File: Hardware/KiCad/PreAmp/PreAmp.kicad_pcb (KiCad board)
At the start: 2 copper layers, 27 parts, among them J1 XLR3, J2 Conn_01x03_Pin, J3 Conn_01x05_Pin, U1 TLV2371DBV, U2 INA217AIDWR

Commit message: Layout everything globaly
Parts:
- moved R4 66.8 mm to (172.8, 67.0), turned to 90 degrees
- moved R2 51.6 mm to (160.2, 57.5), turned to 0 degrees
- moved TP2 47.6 mm to (172.0, 84.2)
- moved R1 46.9 mm to (156.1, 57.5), turned to 0 degrees
- moved U1 45.7 mm to (158.3, 61.2), turned to 90 degrees
- moved J3 44.3 mm to (140.5, 52.5)
- moved C4 43.2 mm to (151.2, 71.2)
- moved U2 41.8 mm to (158.8, 69.8)
- moved TP3 41.8 mm to (149.8, 67.5)
- moved TP1 41.7 mm to (153.5, 62.2)
- moved C3 40.1 mm to (166.0, 65.2), turned to 90 degrees
- moved J2 39.9 mm to (140.5, 68.5)
- moved R3 39.2 mm to (172.8, 73.3), turned to -90 degrees
- moved R5 21.8 mm to (151.2, 75.2), turned to -90 degrees
- moved RV1 21.2 mm to (161.2, 77.2)
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
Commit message: First layout
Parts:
- removed J3: Conn_01x05_Pin, Connector_PinSocket_2.54mm:PinSocket_1x05_P2.54mm_Vertical
- J2: value Conn_01x03_Pin -> Conn_01x05_Pin; footprint Connector_PinSocket_2.54mm:PinSocket_1x03_P2.54mm_Vertical -> Connector_PinHeader_2.54mm:PinHeader_1x05_P2.54mm_Vertical
- moved J2 5.09 mm to (145.5, 67.5), turned to 180 degrees
- moved D1 0.26 mm to (180.2, 60.4)
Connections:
- J2 pad 1: GND -> Out
- J2 pad 2: Out -> GND
- J2 pad 3: GND -> -6V

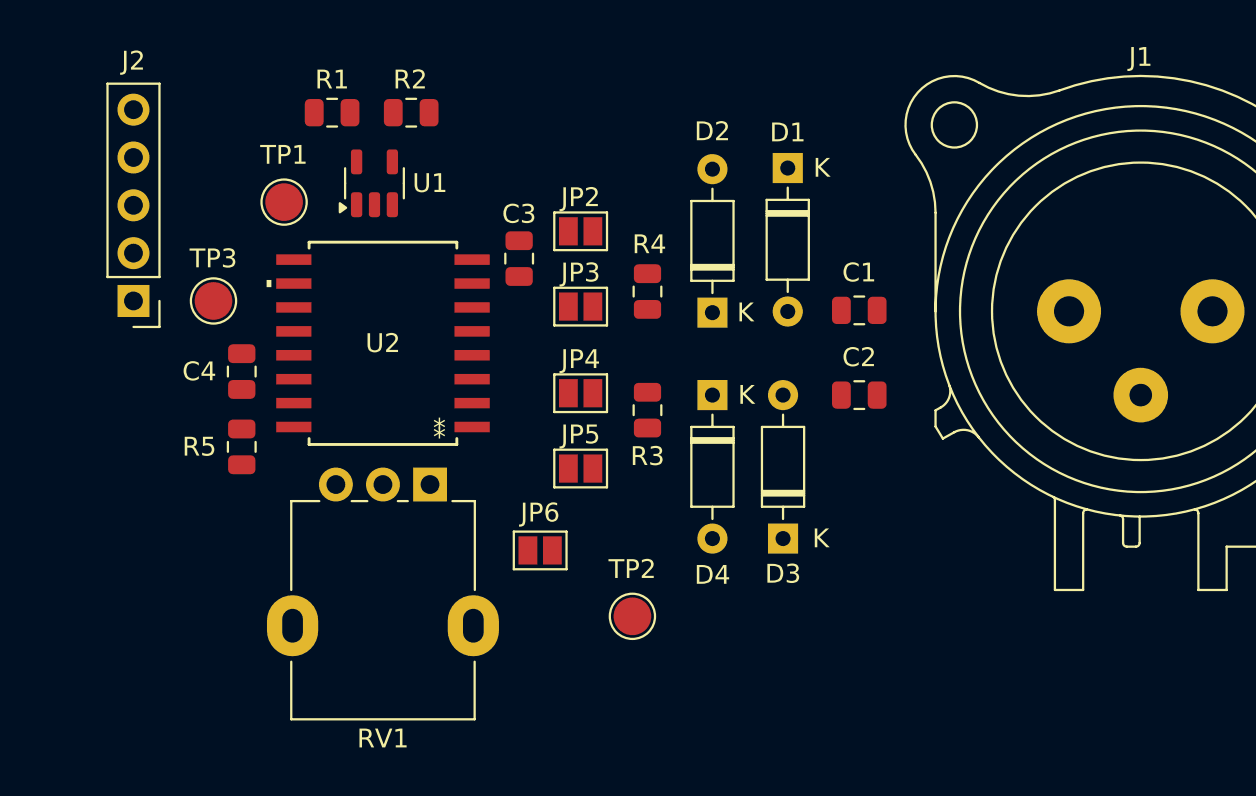
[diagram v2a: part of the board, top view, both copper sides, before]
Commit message: Equal length traces for Hot and Cold
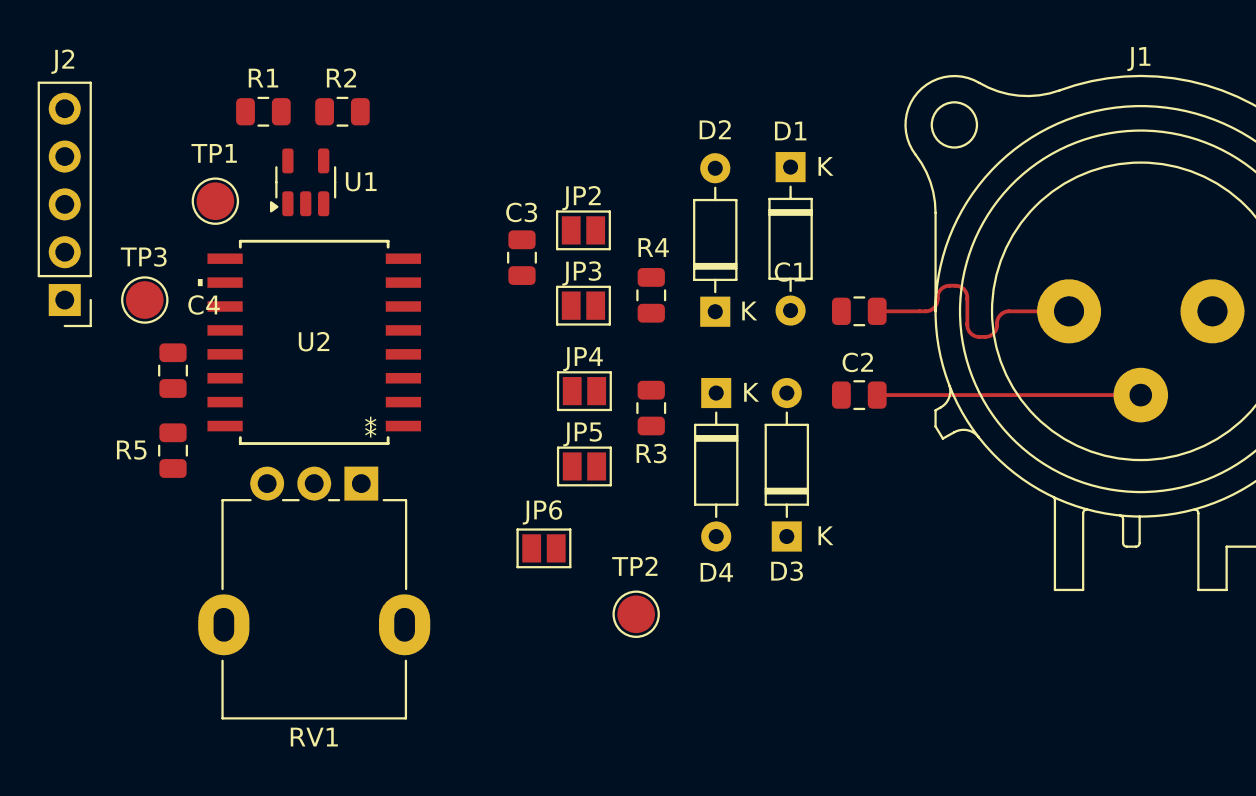
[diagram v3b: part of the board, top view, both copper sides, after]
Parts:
- moved R5 3.66 mm to (147.6, 75.5), turned to 90 degrees
- moved C4 3.65 mm to (147.6, 71.2)
- moved J2 3.65 mm to (141.8, 67.5)
- moved R1 3.65 mm to (152.4, 57.5)
- moved R2 3.65 mm to (156.6, 57.5)
- moved RV1 3.65 mm to (157.6, 77.2)
- moved TP1 3.65 mm to (149.8, 62.2)
- moved TP3 3.65 mm to (146.1, 67.5)
- moved U1 3.65 mm to (154.7, 61.2)
- moved U2 3.65 mm to (155.1, 69.7)
- moved R4 0.28 mm to (173.0, 67.2)
- moved JP6 0.23 mm to (167.3, 80.6)
- moved D3 0.23 mm to (180.2, 80.0)
- moved D4 0.23 mm to (176.4, 72.4)
- moved JP4 0.23 mm to (169.4, 72.3)
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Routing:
- net Cold: track 0.00 -> 14.0 mm
- net Hot: track 0.00 -> 13.8 mm

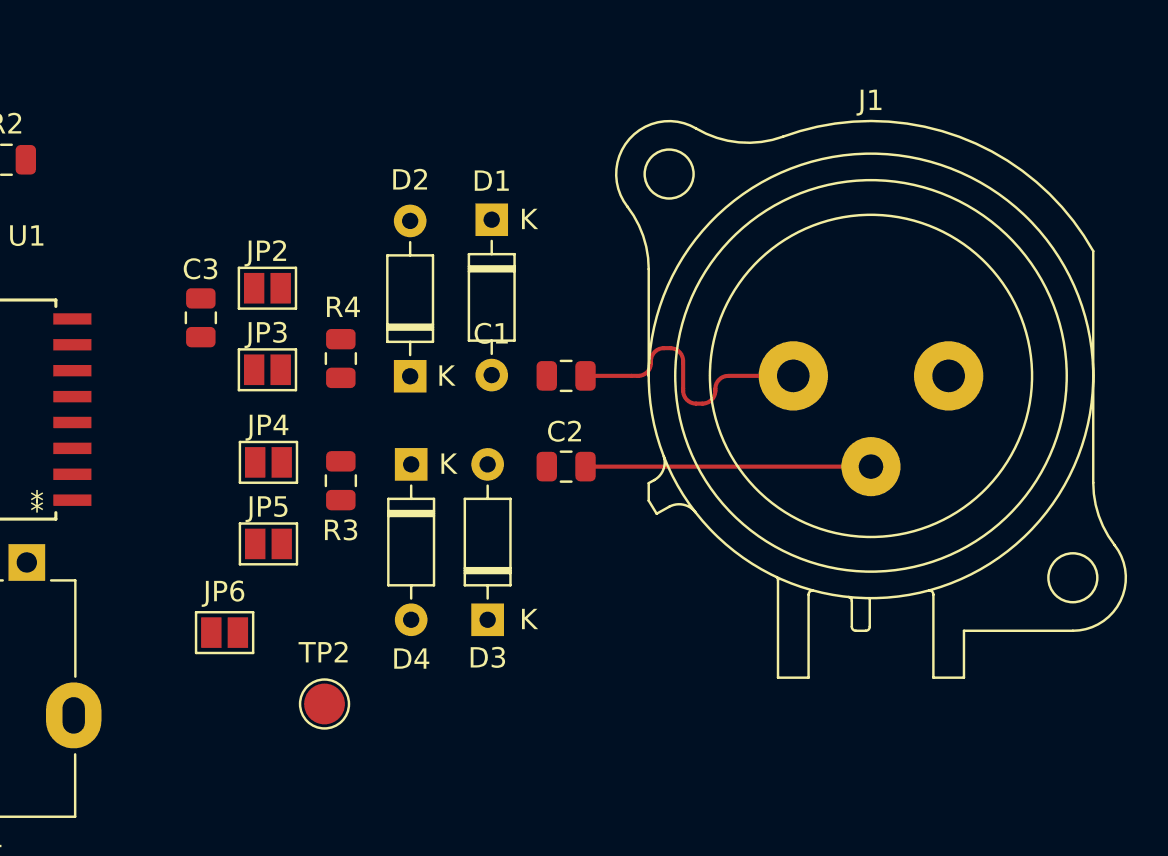
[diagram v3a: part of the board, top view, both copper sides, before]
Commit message: First part of differential routing
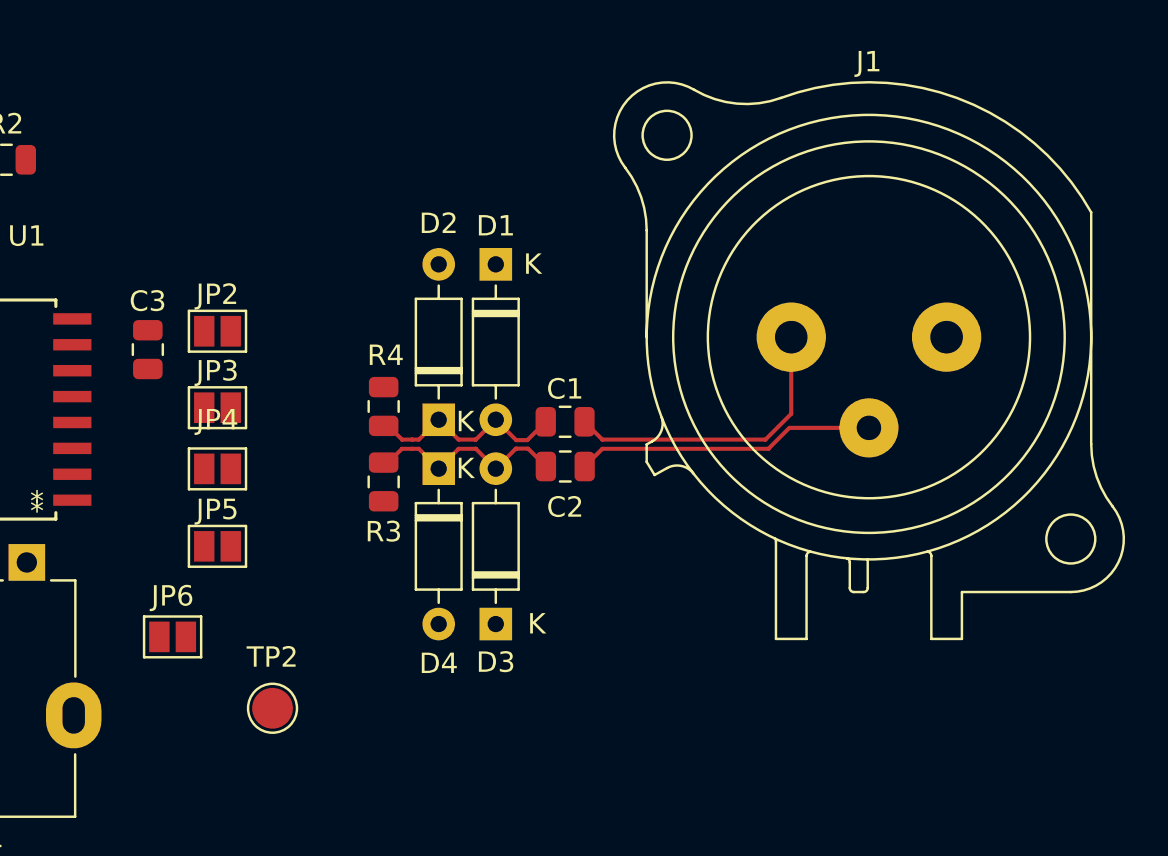
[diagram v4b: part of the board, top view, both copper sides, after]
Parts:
- moved JP2 3.23 mm to (166.9, 65.9)
- moved R4 3.15 mm to (175.1, 69.5)
- moved JP3 3.08 mm to (166.9, 69.6)
- moved C3 3.03 mm to (163.5, 66.8)
- moved JP6 2.56 mm to (164.8, 80.8)
- moved TP2 2.56 mm to (169.7, 84.3)
- moved D2 2.55 mm to (177.8, 70.2)
- moved JP4 2.52 mm to (166.9, 72.6)
- moved JP5 2.50 mm to (166.9, 76.4)
- moved C1 2.25 mm to (184.0, 70.3)
- moved D1 2.20 mm to (180.6, 62.6)
- moved R3 2.10 mm to (175.1, 73.2)
- moved J1 1.90 mm to (202.7, 66.2)
- moved D4 1.37 mm to (177.8, 72.6)
- moved D3 0.45 mm to (180.6, 80.2)
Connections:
- net Cold renamed Input-
- net Hot renamed Input+
- net Net-(D1-A) renamed /In+
- net Net-(D3-A) renamed /In-
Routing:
- net /In+: track 0.00 -> 10.6 mm
- net /In-: track 0.00 -> 10.2 mm
- net Input+: track 13.8 -> 14.8 mm
- net Input-: track 14.0 -> 14.7 mm

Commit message: Removed 4 jumper points
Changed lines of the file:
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@@
 			(layer "F.Fab")
-		)
-		(fp_text user "K"
-			(at 0 -1.3 180)
-			(layer "F.SilkS")
-			(effects
-				(font
-					(size 1 1)
-					(thickness 0.15)
-				)
-			)
 		)
 		(fp_text user "${REFERENCE}"
@@
 		)
 		(fp_text user "K"
-			(at -0.1 1.3 180)
-			(layer "F.SilkS")
-			(effects
-				(font
-					(size 1 1)
-					(thickness 0.15)
-				)
-			)
-		)
-		(fp_text user "K"

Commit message: Connected everything together
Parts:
- removed JP2, JP3, JP4, JP5: SolderJumper_2_Open, Jumper:SolderJumper-2_P1.3mm_Open_Pad1.0x1.5mm
- moved TP2 29.0 mm to (198.5, 87.4)
- moved J2 11.2 mm to (152.9, 69.4)
- moved TP3 10.9 mm to (156.8, 69.4)
- moved C4 10.7 mm to (158.1, 73.0)
- moved R5 10.3 mm to (157.8, 77.0)
- moved U2 10.2 mm to (165.2, 71.4)
- moved RV1 10.2 mm to (167.7, 78.4)
- moved TP1 9.46 mm to (159.2, 63.9)
- moved JP1 9.27 mm to (173.9, 79.7)
- moved C3 8.88 mm to (172.4, 66.2)
- moved R2 8.13 mm to (164.7, 57.2)
- moved R1 8.13 mm to (160.5, 57.2)
- moved U1 8.13 mm to (162.8, 61.0)
- moved J1 0.45 mm to (203.1, 66.0)
- moved C1 0.40 mm to (184.4, 70.3)
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- renumbered JP6 to JP1
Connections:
- net Input+ renamed /Input+
- net Input- renamed /Input-
- U2 pad 4: Net-(JP4-B) -> /In-
- U2 pad 5: Net-(JP2-B) -> /In+
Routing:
- net -6V: track 0.00 -> 56.5 mm, vias 0 -> 2
- net 6V: track 0.00 -> 32.8 mm
- net 1.6V: track 0.00 -> 15.2 mm
- net Out: track 0.00 -> 7.60 mm
- net Net-(U2-RG1): track 0.00 -> 6.32 mm
- net Net-(JP1-A): track 0.00 -> 6.14 mm
- net /In+: track 10.6 -> 16.6 mm
- net /In-: track 10.2 -> 16.3 mm
- net Net-(R5-Pad1): track 0.00 -> 5.07 mm
- net Net-(U1--): track 0.00 -> 4.93 mm
- net Net-(U2-RG2): track 0.00 -> 3.36 mm

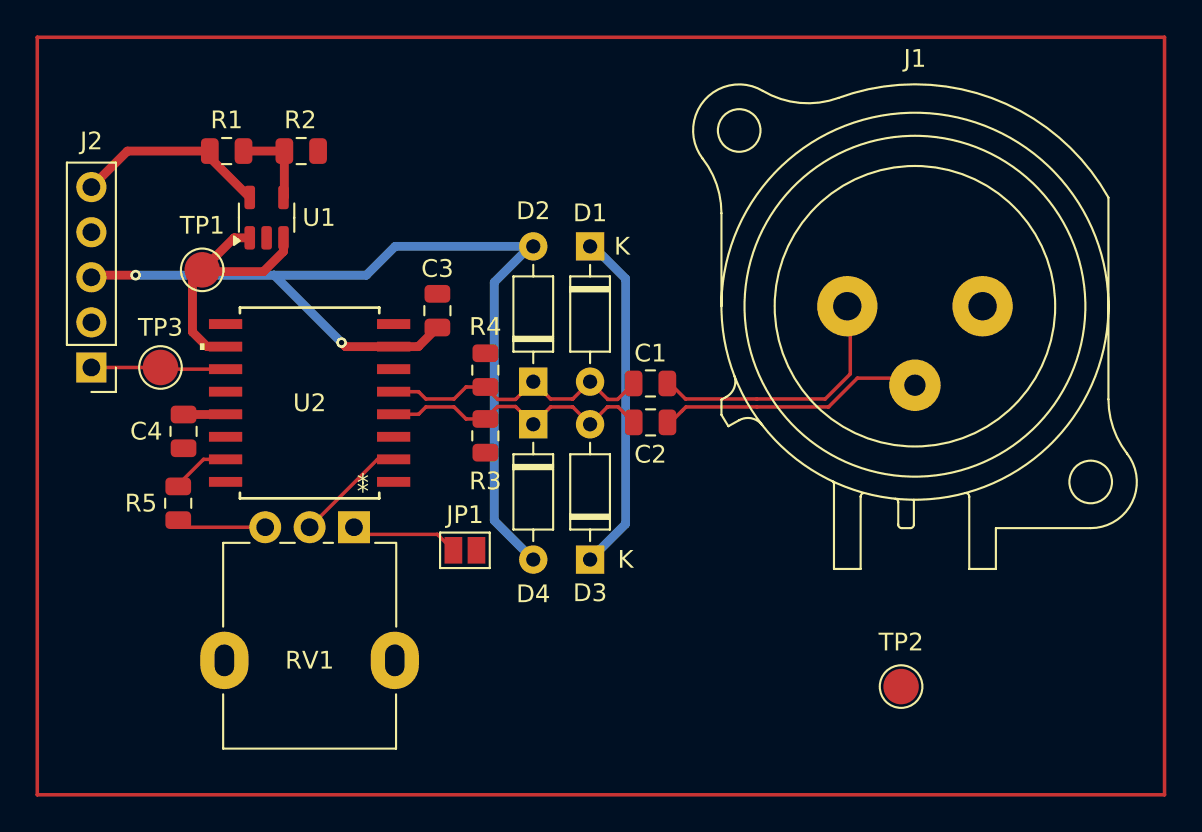
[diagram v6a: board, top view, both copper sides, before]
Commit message: Lower ground plane
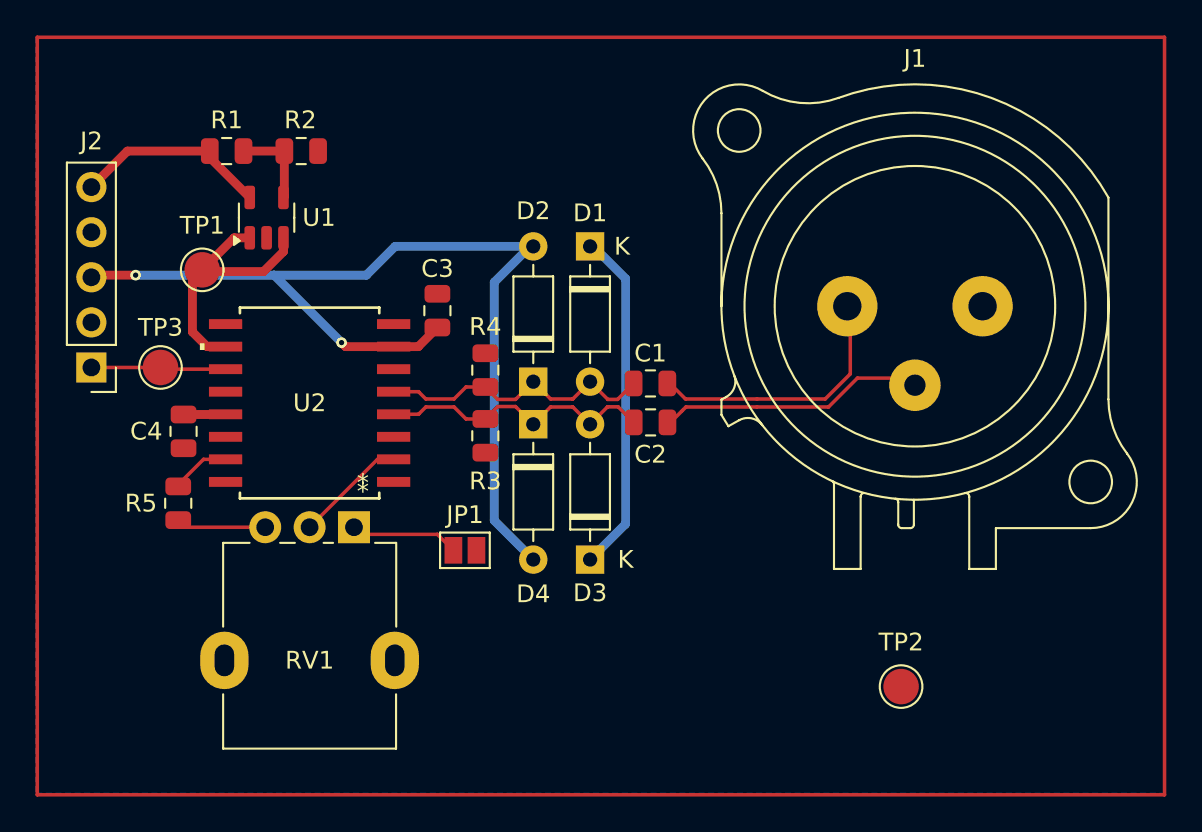
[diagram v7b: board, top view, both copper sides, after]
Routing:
- added copper zone on B.Cu, net GND
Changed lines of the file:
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@@
 	)
 	(segment
-		(start 180.000001 71.625001)
-		(end 180 71.625)
-		(width 0.2)
-		(layer "F.Cu")
-		(net 19)
-	)
-	(segment
-		(start 178.775 71.625)
-		(end 177.8 72.6)
+		(start 177.8 72.6)
+		(end 178.774999 71.625001)
 		(width 0.2)
 		(layer "F.Cu")
@@
 	)
 	(segment
+		(start 178.774999 71.625001)
+		(end 180.025001 71.625001)
+		(width 0.2)
+		(layer "F.Cu")
+		(net 19)
+	)
+	(segment
 		(start 182 71.618029)
 		(end 182.581973 71.618029)
@@
 	)
 	(segment
-		(start 181 72.6)
-		(end 180.025001 71.625001)
-		(width 0.2)
-		(layer "F.Cu")
-		(net 19)
-	)
-	(segment
-		(start 180 71.625)
-		(end 178.775 71.625)
+		(start 180.025001 71.625001)
+		(end 181 72.6)
 		(width 0.2)
 		(layer "F.Cu")
@@
 	)
 	(segment
-		(start 180.025001 71.625001)
-		(end 180.000001 71.625001)
-		(width 0.2)
-		(layer "F.Cu")
-		(net 19)
-	)
-	(segment
 		(start 171.3398 72.035)
 		(end 169.934301 72.035)
@@
 		(net 22)
 	)
+	(zone
+		(net 1)
+		(net_name "GND")
+		(layer "B.Cu")
+		(hatch edge 0.5)
+		(connect_pads
+			(clearance 0.5)
+		)
+		(min_thickness 0.25)
+		(filled_areas_thickness no)
+		(fill yes
+			(thermal_gap 0.5)
+			(thermal_bridge_width 0.5)
+		)
+		(polygon
+			(pts
+				(xy 149.8 93.4) (xy 213.4 93.4) (xy 213.4 50.8) (xy 149.8 50.8)
+			)
+		)
+	)
 	(generated

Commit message: V1 done
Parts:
- moved JP1 43.7 mm to (142.4, 110.0)
- moved R4 43.4 mm to (143.2, 98.9)
- moved R3 43.4 mm to (143.2, 102.6)
- moved C1 43.0 mm to (153.0, 99.7)
- moved C2 43.0 mm to (153.0, 101.9)
- moved D4 43.0 mm to (146.4, 102.0)
- moved R5 43.0 mm to (126.4, 106.4)
- moved R1 43.0 mm to (129.1, 86.6)
- moved R2 43.0 mm to (133.3, 86.6)
- moved U1 43.0 mm to (131.4, 90.3)
- moved C3 43.0 mm to (141.0, 95.6)
- moved D1 43.0 mm to (149.6, 92.0)
- moved D2 43.0 mm to (146.4, 99.6)
- moved D3 43.0 mm to (149.6, 109.6)
- moved J1 43.0 mm to (171.7, 95.3)
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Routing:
- net GND: track 0.00 -> 83.5 mm, vias 0 -> 4
- net 6V: track 32.8 -> 62.9 mm
- net /In-: track 16.3 -> 17.0 mm
- net /In+: track 16.6 -> 17.1 mm
- net -6V: track 56.5 -> 56.7 mm, vias 2 -> 1
- added copper zone on F.Cu, net GND
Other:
- board text added: "K"
